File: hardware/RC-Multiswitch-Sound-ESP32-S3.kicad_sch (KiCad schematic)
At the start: 41 parts, among them CN1 UART A, CN2 12V, CN3 TPA3116D2, J1 Ausgaenge, J2 PCM5102A, J3 MAX98357A, J4 GAIN, J5 UART B, J6 UART C, J7 Setup, J8 SD-VCC, J9 microSD-TF-Modul, U1 ESP32-S3-DevKitC-1 (N16R8), U2 ULN2803A

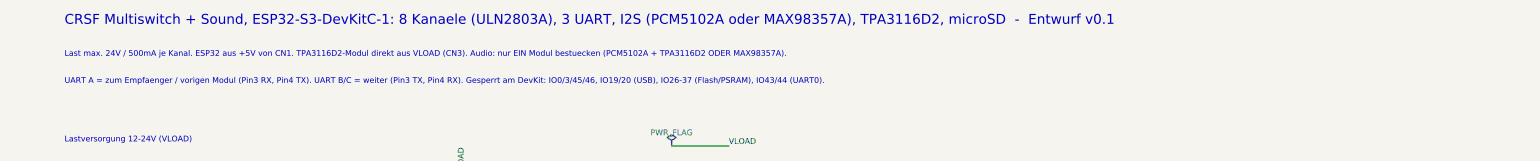
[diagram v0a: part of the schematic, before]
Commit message: Umbenennung CRSF-Multiswitch -> RC-Multiswitch
Neutraler Name, weil der Multiswitch neben CRSF auch SBUS versteht.
README, docs (MD und DOCX), KiCad-Projekt (Dateinamen, Projekt- und
Sheet-Verweise, Titel), Sketch-Ordner und CI-Pfad angepasst.
Geraetename, WLAN-SSID und Config-Export bleiben "MultiSwitch".

Co-Authored-By: Claude Opus 5.5 (1M context) <noreply@anthropic.com>
Claude-Session: https://claude.ai/code/session_01Np9GkYmRMGJmd89YiKPa21
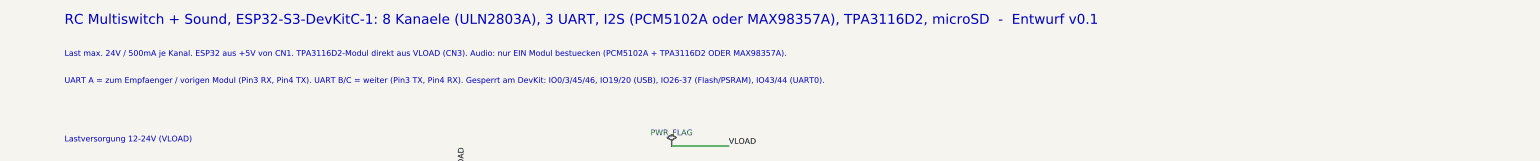
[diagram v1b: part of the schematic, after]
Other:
- note added: "RC Multiswitch + Sound, ESP32-S3-DevKitC-1: 8 Kanaele (ULN2803A), 3 UART, I2S (PCM5102A oder MAX98357A), TPA3116D2, microSD - Entwurf v0.1"
- note removed: "CRSF Multiswitch + Sound, ESP32-S3-DevKitC-1: 8 Kanaele (ULN2803A), 3 UART, I2S (PCM5102A oder MAX98357A), TPA3116D2, microSD - Entwurf v0.1"
- title: CRSF Multiswitch + Sound ESP32-S3 (ULN2803A, I2S, microSD) -> RC Multiswitch + Sound ESP32-S3 (ULN2803A, I2S, microSD)

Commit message: Lokale KiCad-Staende vom 2026-10-17/18 uebernehmen
Die Arbeit lag nur lokal (nicht auf GitHub) und wurde beim Abgleich
nach der Umbenennung ueberschrieben. Wiederhergestellt aus
backups/vor-umbenennung, Dateinamen und Projektverweise auf
RC-Multiswitch angepasst.

Co-Authored-By: Claude Opus 5.5 (1M context) <noreply@anthropic.com>
Claude-Session: https://claude.ai/code/session_01Np9GkYmRMGJmd89YiKPa21
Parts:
- removed CN3: TPA3116D2, Connector_JST:JST_PH_S2B-PH-K_1x02_P2.00mm_Horizontal, symbol local:Conn_TPA_Pwr
- removed J3: MAX98357A, Connector_PinHeader_2.54mm:PinHeader_1x07_P2.54mm_Vertical, symbol local:Mod_MAX98357A
- removed J4: GAIN, Connector_PinHeader_2.54mm:PinHeader_1x03_P2.54mm_Vertical, symbol local:Jumper_Gain
- removed J7: Setup, Connector_PinHeader_2.54mm:PinHeader_1x02_P2.54mm_Vertical, symbol local:Conn_Setup
- removed J8: SD-VCC, Connector_PinHeader_2.54mm:PinHeader_1x03_P2.54mm_Vertical, symbol local:Jumper_SDVcc
- removed R17: 100k, Resistor_THT:R_Axial_DIN0207_L6.3mm_D2.5mm_P7.62mm_Horizontal, symbol Device:R
- added CN4: Lautsprecher, Connector_JST:JST_PH_S2B-PH-K_1x02_P2.00mm_Horizontal, symbol local:Conn_Speaker
- added J11: TPA3118 HW-327, ESP32-S3-DevKitC-1_THT:Mod_TPA3118_HW327_THT, symbol local:Mod_TPA3118
- CN2: value 12V -> 3S
- D1: value P6KE33A -> P6KE15A
- J2: footprint Connector_PinHeader_2.54mm:PinHeader_1x06_P2.54mm_Vertical -> ESP32-S3-DevKitC-1_THT:Mod_PCM5102A_GY_THT
- J9: footprint Connector_PinHeader_2.54mm:PinHeader_1x06_P2.54mm_Vertical -> ESP32-S3-DevKitC-1_THT:Mod_microSD_SPI_THT
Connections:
- net SD_VCC is gone; now on net +3V3: J9.1 (VCC)
- net GND: now also J2.7 (AGND), J2.9 (AGND), J11.2 (GND), J11.4 (PWR-)
- net VLOAD: now also J11.3 (PWR+)
- net AMP_SD: no longer names the net of U1.12 (IO8)
- net SETUP: no longer names the net of U1.15 (IO9)
- new net: CN4.1 (SPK+), J11.5 (OUT+)
- new net: CN4.2 (SPK-), J11.6 (OUT-)
- new net AUDIO_MONO: J11.1 (IN), J2.10 (L)
- no-connect marks 0 -> 3
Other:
- note added: "AUDIO: PCM5102A + TPA3118"
- note added: "Lastversorgung 3S LiPo 9-12,6 V (VLOAD)"
- note added: "Line-Out: Pad L (J2 Pin 10) direkt als Mono-Signal -> J11; R-Pad nicht benutzt (Quelle ist mono)"
- note added: "Modul-MUTE offen lassen; Versorgung nur aus VLOAD (Modul 8-24 V: 3S-Akku nicht unter ca. 9 V entladen)"
- note added: "PCM5102A (6-pol.), SCK fest auf GND"
- note added: "PCM5102A: Loetbruecken H1L-H4L am Modul lt. Datenblatt pruefen (typ. FLT=L, DEMP=L, XSMT=H, FMT=L); SCK an GND (fest)"
- note added: "RC Multiswitch + Sound, ESP32-S3-DevKitC-1: 8 Kanaele (ULN2803A), 3 UART, I2S (PCM5102A), TPA3118, microSD - Entwurf v0.8"
- note added: "TPA3118 (HW-327, MONO): Modul wird auf die Platine geloetet (J11: IN, GND, PWR+, PWR-, OUT+, OUT-), Versorgung aus VLOAD, Lautsprecher an CN4 (JST PH 2). MUTE-Pads offen"
- note added: "Versorgung 3S LiPo (9-12,6 V), max. 500mA je Kanal. ESP32 aus +5V von CN1. TPA3118-Modul direkt aus VLOAD (J11), Lautsprecher an CN4. Audio: PCM5102A + TPA3118."
- note added: "microSD TF-Card-Modul (6-pol., SPI auf IO10-13), VCC = 3V3 vom ESP32-Board (reines 3,3V-Modul!)"
- note removed: "(Module mit Spannungsregler/Pegelwandler: 5V, reine 3V3-Module: 3V3)"
- note removed: "+5V = 6dB"
- note removed: "A) PCM5102A (6-pol.), SCK fest auf GND"
- note removed: "AUDIO (nur eine Variante bestuecken)"
- note removed: "B) MAX98357A (7-pol.)"
- note removed: "CN3 -> Versorgung TPA3116D2-Modul (+ / -)"
- note removed: "J4: GND = 12dB, offen = 9dB,"
- note removed: "J7: Setup-Taster (IO9)"
- note removed: "J8: Jumper 3V3 oder 5V je nach Modul"
- note removed: "Last max. 24V / 500mA je Kanal. ESP32 aus +5V von CN1. TPA3116D2-Modul direkt aus VLOAD (CN3). Audio: nur EIN Modul bestuecken (PCM5102A + TPA3116D2 ODER MAX98357A)."
- note removed: "Lastversorgung 12-24V (VLOAD)"
- note removed: "Lautsprecher direkt am Modul"
- note removed: "Line-Out per Kabel zum TPA3116D2"
- note removed: "R17: Pull-down, stumm"
- note removed: "RC Multiswitch + Sound, ESP32-S3-DevKitC-1: 8 Kanaele (ULN2803A), 3 UART, I2S (PCM5102A oder MAX98357A), TPA3116D2, microSD - Entwurf v0.1"
- note removed: "beim Booten (IO8)"
- note removed: "microSD TF-Card-Modul (6-pol., SPI auf IO10-13)"

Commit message: Widerstandswerte R1-R16 entfernt, Anwender legt sie aus
- R1-R16 ohne Wert (Schaltplan + PCB), Hinweis im Schaltplan angepasst
- Projektbeschreibung, README, README-hardware: Anwender legt Werte selbst aus, LED-Empfehlung im Schaltplan
- D1 P6KE15A und 3S-Versorgung bleiben (TPA3118 braucht >= 8 V)

Co-Authored-By: Claude Opus 5.5 (1M context) <noreply@anthropic.com>
Claude-Session: https://claude.ai/code/session_015ZTAHN4h1MhX6WfGWCfmx3
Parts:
- R1, R10, R11, R12, R13, R14, R15, R16, R2, R3, R4, R5, R6, R7, R8, R9: value 150 -> R
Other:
- note added: "Ausgangswiderstaende (THT, Werte legt der Anwender je Verbraucher fest)"
- note removed: "Ausgangswiderstaende (THT, je Verbraucher waehlen)"
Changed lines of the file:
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@@
 		)
 	)
-	(text "Ausgangswiderstaende (THT, je Verbraucher waehlen)"
+	(text "Ausgangswiderstaende (THT, Werte legt der Anwender je Verbraucher fest)"
 		(exclude_from_sim no)
 		(at 190 78 0)
@@
 			)
 		)
-		(property "Value" "150"
+		(property "Value" "R"
 			(at 124.46 132.54 270)
 			(effects
@@
 			)
 		)
-		(property "Value" "150"
+		(property "Value" "R"
 			(at 218.44 86.82 270)
 			(effects
@@
 			)
 		)
-		(property "Value" "150"
+		(property "Value" "R"
 			(at 124.46 140.16 270)
 			(effects
@@
 			)
 		)
-		(property "Value" "150"
+		(property "Value" "R"
 			(at 218.44 109.68 270)
 			(effects
@@
 			)
 		)
-		(property "Value" "150"
+		(property "Value" "R"
 			(at 124.46 94.44 270)
 			(effects
@@
 			)
 		)
-		(property "Value" "150"
+		(property "Value" "R"
 			(at 218.44 102.06 270)
 			(effects
@@
 			)
 		)
-		(property "Value" "150"
+		(property "Value" "R"
 			(at 218.44 124.92 270)
 			(effects
@@
 			)
 		)
-		(property "Value" "150"
+		(property "Value" "R"
 			(at 218.44 117.3 270)
 			(effects
@@
 			)
 		)
-		(property "Value" "150"
+		(property "Value" "R"
 			(at 124.46 124.92 270)
 			(effects
@@
 			)
 		)
-		(property "Value" "150"
+		(property "Value" "R"
 			(at 124.46 117.3 270)
 			(effects
@@
 			)
 		)
-		(property "Value" "150"
+		(property "Value" "R"
 			(at 218.44 140.16 270)
 			(effects
@@
 			)
 		)
-		(property "Value" "150"
+		(property "Value" "R"
 			(at 124.46 109.68 270)
 			(effects
@@
 			)
 		)
-		(property "Value" "150"
+		(property "Value" "R"
 			(at 218.44 132.54 270)
 			(effects
@@
 			)
 		)
-		(property "Value" "150"
+		(property "Value" "R"
 			(at 218.44 94.44 270)
 			(effects
@@
 			)
 		)
-		(property "Value" "150"
+		(property "Value" "R"
 			(at 124.46 86.82 270)
 			(effects
@@
 			)
 		)
-		(property "Value" "150"
+		(property "Value" "R"
 			(at 124.46 102.06 270)
 			(effects

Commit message: Schaltplan v0.9: Lastmasse GNDPWR mit NetTie, Netzklassen und DRC-Regeln
- ULN2803 Pin 9 an eigenes Netz GNDPWR, Verbindung zu GND nur ueber
  NetTie NT1 (im PCB direkt an CN2 Pin 1 platzieren), PWR_FLAG an GNDPWR
- Netzklassen: Power 1,5 mm (GND, GNDPWR, /VLOAD, Lautsprecher CN4),
  Kanal 0,5 mm (/OUT*)
- kicad_dru: Mindestbreite Power 1,0 mm, Kanal 0,4 mm
- README-hardware ergaenzt; PCB unveraendert

Co-Authored-By: Claude Opus 5.5 (1M context) <noreply@anthropic.com>
Claude-Session: https://claude.ai/code/session_018bh1aktNNbeTvdMLiwxhbB
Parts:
- added NT1: NetTie GND/GNDPWR, NetTie:NetTie-2_SMD_Pad2.0mm, symbol Device:NetTie_2
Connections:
- net GND: now also NT1.1; no longer U2.9 (GND)
- new net GNDPWR: NT1.2, U2.9 (GND)
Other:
- note added: "GNDPWR = Lastmasse ULN2803 (Pin 9), eigene breite Bahn direkt zu NT1/CN2"
- note added: "NT1: einzige Verbindung GND <-> GNDPWR (Sternpunkt). Im PCB direkt an CN2 Pin 1 platzieren."

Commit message: Hardware: TBD62083APG statt ULN2803A
ULN2803A ist abgekuendigt. Der TBD62083APG (DMOS) hat dieselbe Pinbelegung und passt in denselben Sockel, Leiterbahnen und Netze bleiben unveraendert. Schaltplan-Symbol, Bauteilwert, Bestueckungsdruck und Doku angepasst.

Co-Authored-By: Claude Opus 5.5 <noreply@anthropic.com>
Claude-Session: https://claude.ai/code/session_0118D4qppRkb6gR5m3R2CZyV
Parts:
- U2: value ULN2803A -> TBD62083APG; symbol Transistor_Array:ULN2803A -> local:TBD62083APG
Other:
- note added: "GNDPWR = Lastmasse TBD62083APG (Pin 9), eigene breite Bahn direkt zu NT1/CN2"
- note added: "RC Multiswitch + Sound, ESP32-S3-DevKitC-1: 8 Kanaele (TBD62083APG), 3 UART, I2S (PCM5102A), TPA3118, microSD - Entwurf v0.8"
- note removed: "GNDPWR = Lastmasse ULN2803 (Pin 9), eigene breite Bahn direkt zu NT1/CN2"
- note removed: "RC Multiswitch + Sound, ESP32-S3-DevKitC-1: 8 Kanaele (ULN2803A), 3 UART, I2S (PCM5102A), TPA3118, microSD - Entwurf v0.8"
- title: RC Multiswitch + Sound ESP32-S3 (ULN2803A, I2S, microSD) -> RC Multiswitch + Sound ESP32-S3 (TBD62083APG, I2S, microSD)
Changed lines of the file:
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@@
 	(paper "A3")
 	(title_block
-		(title "RC Multiswitch + Sound ESP32-S3 (ULN2803A, I2S, microSD)")
+		(title "RC Multiswitch + Sound ESP32-S3 (TBD62083APG, I2S, microSD)")
 		(date "2026-10-19")
 		(rev "v0.9")
@@
 		(comment 7 "v0.7: TPA3118-Modul wird eingeloetet (J11 mit 6 Pads, Footprint Mod_TPA3118_HW327_THT), CN3 entfaellt, Lautsprecherausgang als JST PH CN4")
 		(comment 8 "v0.8: Betrieb max. 3S LiPo (9-12,6 V): TVS D1 P6KE33A -> P6KE15A, Beschriftungen angepasst")
-		(comment 9 "v0.9: Lastmasse GNDPWR (ULN2803 Pin 9) ueber NetTie NT1 an CN2, Netzklassen Power/Kanal")
+		(comment 9 "v0.9: Lastmasse GNDPWR (TBD62083APG Pin 9) ueber NetTie NT1 an CN2, Netzklassen Power/Kanal")
 	)
 	(text "D1: TVS Anode GND, Kathode VLOAD"
@@
 		)
 	)
-	(text "RC Multiswitch + Sound, ESP32-S3-DevKitC-1: 8 Kanaele (ULN2803A), 3 UART, I2S (PCM5102A), TPA3118, microSD  -  Entwurf v0.8"
+	(text "RC Multiswitch + Sound, ESP32-S3-DevKitC-1: 8 Kanaele (TBD62083APG), 3 UART, I2S (PCM5102A), TPA3118, microSD  -  Entwurf v0.8"
 		(exclude_from_sim no)
 		(at 15 14 0)
@@
 	)
 	(symbol
-		(lib_id "Transistor_Array:ULN2803A")
+		(lib_id "local:TBD62083APG")
 		(at 165.1 109.22 0)
 		(unit 1)
@@
 			)
 		)
-		(property "Value" "ULN2803A"
+		(property "Value" "TBD62083APG"
 			(at 165.1 130.5 0)
 			(effects
@@
 		)
 	)
-	(text "GNDPWR = Lastmasse ULN2803 (Pin 9),\neigene breite Bahn direkt zu NT1/CN2"
+	(text "GNDPWR = Lastmasse TBD62083APG (Pin 9),\neigene breite Bahn direkt zu NT1/CN2"
 		(exclude_from_sim no)
 		(at 170.18 134.62 0)
